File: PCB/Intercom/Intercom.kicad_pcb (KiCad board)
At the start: 2 copper layers, 70 x 70 mm, 73 parts, among them J1 Reset, J2 JST-PH-SM4-TB, J4 TC2030-USB-NL-DS, J5 USB-C-Socket-H, P1 Square, P2 Square, SW1 SW_SPST, U1 MD8942, U2 ESP32-S3-MINI-1, U4 ICS43434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

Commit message: Silk
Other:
- board text added: "ESP32-S3-MINI-1-N4R2"
- board text added: "MIC(R)"
- board text added: "SPK(L+R)"
- board text removed: "MIC"

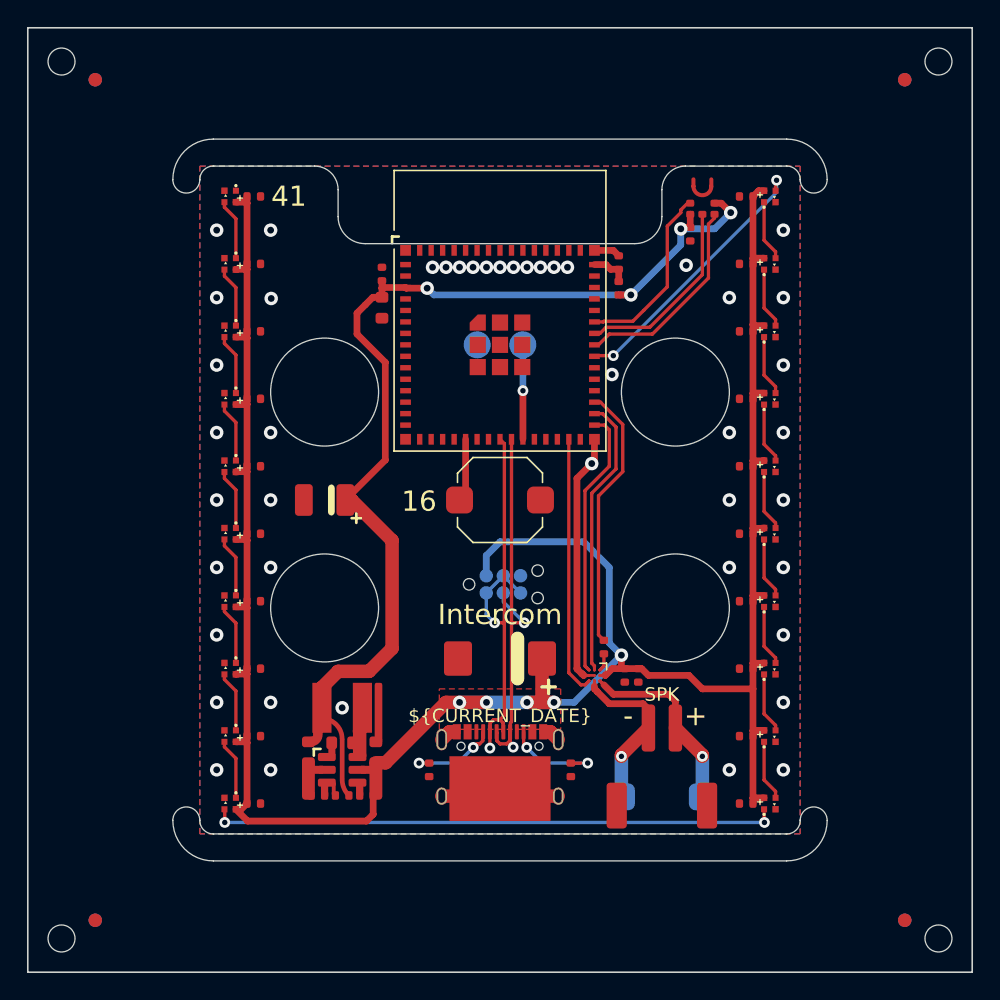
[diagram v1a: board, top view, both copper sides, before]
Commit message: Power control for LEDs
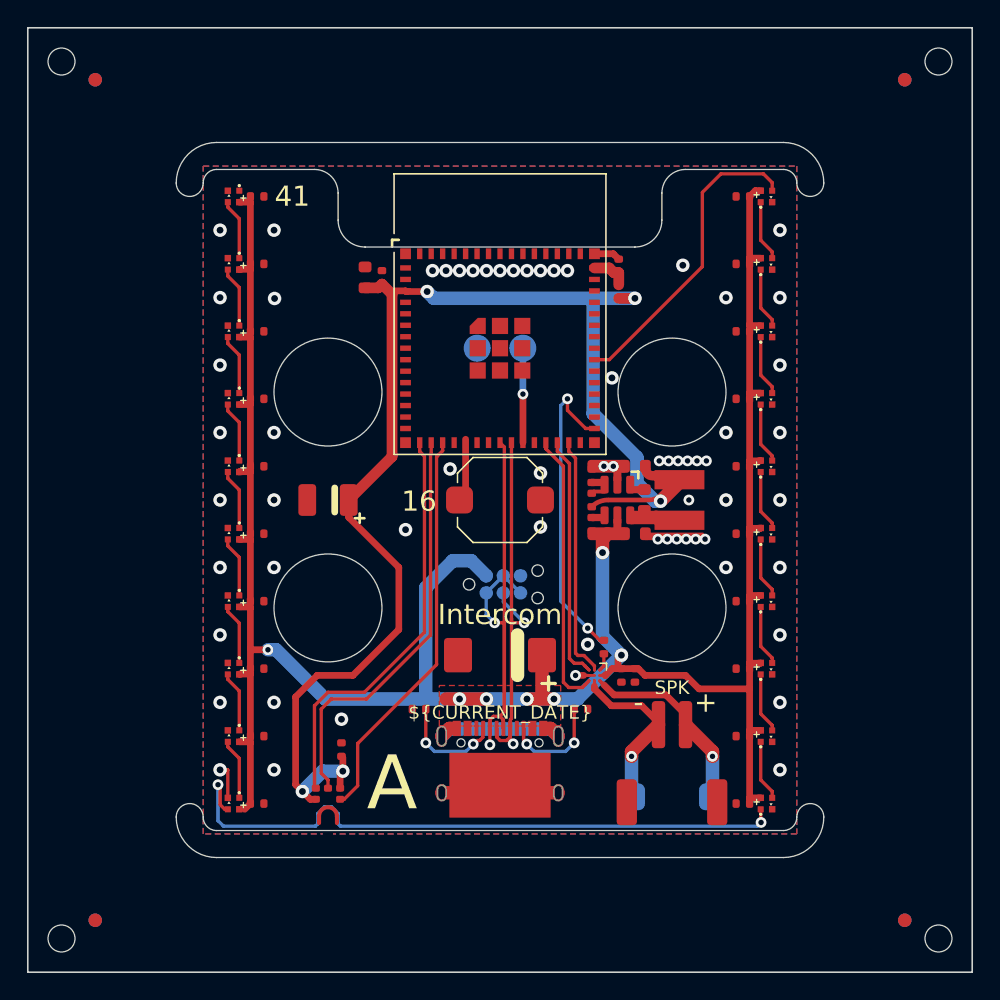
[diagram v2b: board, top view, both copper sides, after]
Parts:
- moved U4 53.0 mm to (87.2, 122.7), turned to -90 degrees
- moved C10 46.1 mm to (88.2, 118.5), turned to -90 degrees
- moved C2 32.2 mm to (110.0, 97.5), turned to 180 degrees
- moved R2 31.2 mm to (106.8, 98.2), turned to 90 degrees
- moved L1 29.4 mm to (113.3, 100.0), turned to 90 degrees
- moved C3 28.7 mm to (110.7, 100.0), turned to 90 degrees
- moved R1 28.7 mm to (106.8, 100.0), turned to 90 degrees
- moved U1 28.6 mm to (108.7, 100.0), turned to 90 degrees
- moved R3 26.1 mm to (106.8, 101.8), turned to 90 degrees
- moved C1 25.1 mm to (110.0, 102.5), turned to 180 degrees
- moved R7 4.56 mm to (94.0, 115.5), turned to 180 degrees
- moved R8 4.56 mm to (106.0, 115.5), turned to 180 degrees
- moved C16 2.57 mm to (90.0, 83.5), turned to 90 degrees
- moved J2 0.79 mm to (112.8, 119.5)
- moved P1 0.75 mm to (115.8, 122.0)
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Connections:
- U2 pad 16: unconnected-(U2-GPIO12-Pad16) -> MICWS
- U2 pad 17: unconnected-(U2-GPIO13-Pad17) -> MICSD
- U2 pad 18: unconnected-(U2-GPIO14-Pad18) -> MICSCK
- U2 pad 27: unconnected-(U2-GPIO47-Pad27) -> SPKLRC
- U2 pad 28: unconnected-(U2-GPIO33-Pad28) -> SPKBSCK
- U2 pad 29: SPKLRC -> SPKDATA
- U2 pad 31: SPKBSCK -> SPKPWR
- U2 pad 32: SPKDATA -> unconnected-(U2-GPIO36-Pad32)
- U2 pad 33: SPKPWR -> unconnected-(U2-GPIO37-Pad33)
- U2 pad 38: MICWS -> unconnected-(U2-GPIO42-Pad38)
- U2 pad 39: MICSD -> unconnected-(U2-GPIO43-Pad39)
- U2 pad 40: MICSCK -> unconnected-(U2-GPIO44-Pad40)
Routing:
- net +3V3: track 73.6 -> 94.1 mm, vias 4 -> 5
- net MICSD: track 14.3 -> 30.7 mm
- net MICSCK: track 13.5 -> 29.8 mm
- net MICWS: track 15.4 -> 30.8 mm
- net Net-(D10-O): track 42.0 -> 48.5 mm
- net D-: track 31.6 -> 37.5 mm
- net GND: track 31.6 -> 25.7 mm, vias 45 -> 64
- net SPKPWR: track 19.7 -> 23.0 mm, vias 0 -> 2
- net SPKDATA: track 20.5 -> 17.6 mm
- net +5V: track 179.0 -> 181.8 mm, vias 5 -> 7
- net LED: track 20.2 -> 23.0 mm, vias 2 -> 0
- net SPKBSCK: track 19.5 -> 17.8 mm
- net SPKLRC: track 18.9 -> 20.1 mm
- net Net-(J5-CC2): track 6.50 -> 7.76 mm
- net Net-(J5-CC1): track 6.84 -> 7.99 mm
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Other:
- board text added: "12 13 14"
- board text added: "47 33 34 35"
- board text added: "5V"
- board text removed: "34 35 36 37"
- board text removed: "42 43 44"
- board text removed: "SPK(L+R)"
